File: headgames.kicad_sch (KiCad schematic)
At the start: 42 parts, among them J1 ELECTRODES, J2 9V ISOLATED BATTERY, U1 TLC274CN LOW-BIAS CMOS, U2 LM386

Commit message: Restore the inventory-first LM324N implementation
Undo the unavailable TLC274CN population decision while preserving the independently valid power-interface, alpha-band, detector, and verification improvements. Restore LM324N consistently across all five schematic units, the title block, README, and architectural guidance.

Make the inventory constraint executable by changing the root verification entrypoint to require LM324N for U1. Document its bipolar input-bias, offset, and noise limitations honestly at the 10 MΩ acquisition impedance, and retain a clean future replacement boundary without making an unstocked part mandatory for the MVP.

Verification: python3 manage.py test passes; KiCad ERC reports zero violations; native PDF export succeeds; git diff --check passes.
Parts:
- U1: value TLC274CN LOW-BIAS CMOS -> LM324N INVENTORY
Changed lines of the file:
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@@
 		(company "Headgames")
 		(comment 1 "BATTERY ONLY WHILE ELECTRODES ARE CONNECTED")
-		(comment 2 "TLC274CN reference, acquisition, alpha gain, and carrier")
+		(comment 2 "LM324N reference, acquisition, alpha gain, and carrier")
 		(comment 3 "Pins 1 and 8 of LM386 intentionally open for gain 20")
 		(comment 4 "Experimental prototype - not a medical device")
@@
 			)
 		)
-		(property "Value" "TLC274CN LOW-BIAS CMOS"
+		(property "Value" "LM324N INVENTORY"
 			(at 88.9 69.1896 0)
 			(effects
@@
 			)
 		)
-		(property "Value" "TLC274CN LOW-BIAS CMOS"
+		(property "Value" "LM324N INVENTORY"
 			(at 165.1 84.4296 0)
 			(effects
@@
 			)
 		)
-		(property "Value" "TLC274CN LOW-BIAS CMOS"
+		(property "Value" "LM324N INVENTORY"
 			(at 45.9232 82.423 0)
 			(effects
@@
 			)
 		)
-		(property "Value" "TLC274CN LOW-BIAS CMOS"
+		(property "Value" "LM324N INVENTORY"
 			(at 161.29 141.5796 0)
 			(effects
@@
 			)
 		)
-		(property "Value" "TLC274CN LOW-BIAS CMOS"
+		(property "Value" "LM324N INVENTORY"
 			(at 232.41 139.0396 0)
 			(effects

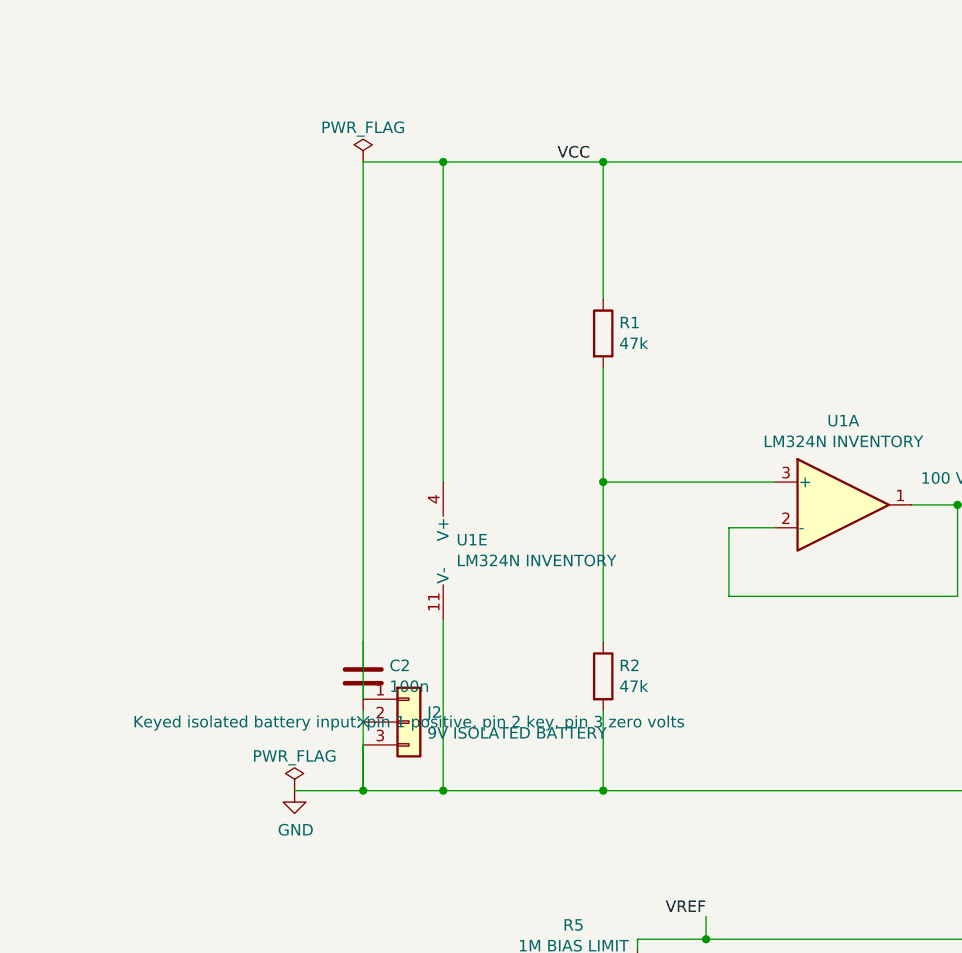
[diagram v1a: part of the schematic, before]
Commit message: Separate the battery inlet from supply decoupling
Move J2 into a dedicated inlet block at the far left of the schematic and route its positive and return conductors around the outside of the circuit. The keyed pin now has an isolated, visible no-connect marker, and neither battery conductor passes through a component body or field.

Restore C2 as an independent vertical bypass branch directly between VCC and ground. Shorten J2's displayed value to avoid colliding with C2 while retaining the complete polarity, keying, and isolation contract in the connector description and the on-sheet safety annotation.

Update the durable J2 value assertion to match the concise displayed field. Verification includes visual inspection of a fresh 3200-pixel native SVG render, successful PDF and netlist exports, zero KiCad ERC violations, passing root engineering checks, and git diff --check.
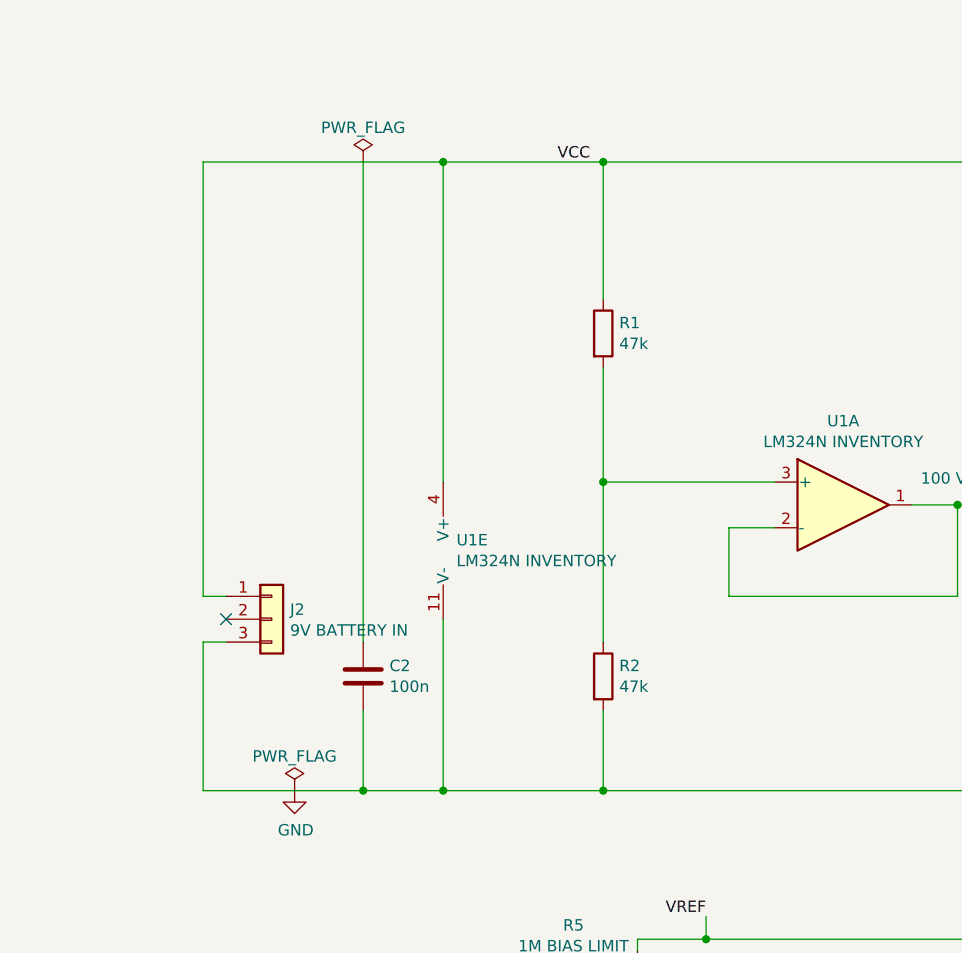
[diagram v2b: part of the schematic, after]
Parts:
- J2: value 9V ISOLATED BATTERY -> 9V BATTERY IN
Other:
- moved on the sheet: J2
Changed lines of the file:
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@@
 	)
 	(no_connect
-		(at 35.56 100.33)
+		(at 20.32 88.9)
 	)
 	(wire
 		(pts
-			(xy 35.56 91.44) (xy 35.56 97.79)
+			(xy 20.32 86.36) (xy 17.78 86.36)
 		)
 		(stroke (width 0) (type default))
@@
 	(wire
 		(pts
-			(xy 35.56 102.87) (xy 35.56 107.95)
+			(xy 17.78 86.36) (xy 17.78 38.1)
+		)
+		(stroke (width 0) (type default))
+	)
+	(wire
+		(pts
+			(xy 17.78 38.1) (xy 35.56 38.1)
+		)
+		(stroke (width 0) (type default))
+	)
+	(wire
+		(pts
+			(xy 20.32 91.44) (xy 17.78 91.44)
+		)
+		(stroke (width 0) (type default))
+	)
+	(wire
+		(pts
+			(xy 17.78 91.44) (xy 17.78 107.95)
+		)
+		(stroke (width 0) (type default))
+	)
+	(wire
+		(pts
+			(xy 17.78 107.95) (xy 27.94 107.95)
 		)
 		(stroke (width 0) (type default))
@@
 	(symbol
 		(lib_id "Connector_Generic:Conn_01x03")
-		(at 40.64 100.33 0)
+		(at 25.4 88.9 0)
 		(unit 1)
 		(exclude_from_sim no)
@@
 		(dnp no)
 		(property "Reference" "J2"
-			(at 42.672 99.2632 0)
+			(at 27.432 87.8332 0)
 			(effects (font (size 1.27 1.27)) (justify left))
 		)
-		(property "Value" "9V ISOLATED BATTERY"
-			(at 42.672 101.5746 0)
+		(property "Value" "9V BATTERY IN"
+			(at 27.432 90.1446 0)
 			(effects (font (size 1.27 1.27)) (justify left))
 		)
 		(property "Footprint" ""
-			(at 40.64 100.33 0)
+			(at 25.4 88.9 0)
 			(effects (font (size 1.27 1.27)))
 		)
 		(property "Datasheet" ""
-			(at 40.64 100.33 0)
+			(at 25.4 88.9 0)
 			(effects (font (size 1.27 1.27)))
 		)
 		(property "Description" "Keyed isolated battery input: pin 1 positive, pin 2 key, pin 3 zero volts"
-			(at 40.64 100.33 0)
-			(effects (font (size 1.27 1.27)))
+			(at 25.4 88.9 0)
+			(effects (font (size 1.27 1.27)) (hide yes))
 		)
 		(pin "1")

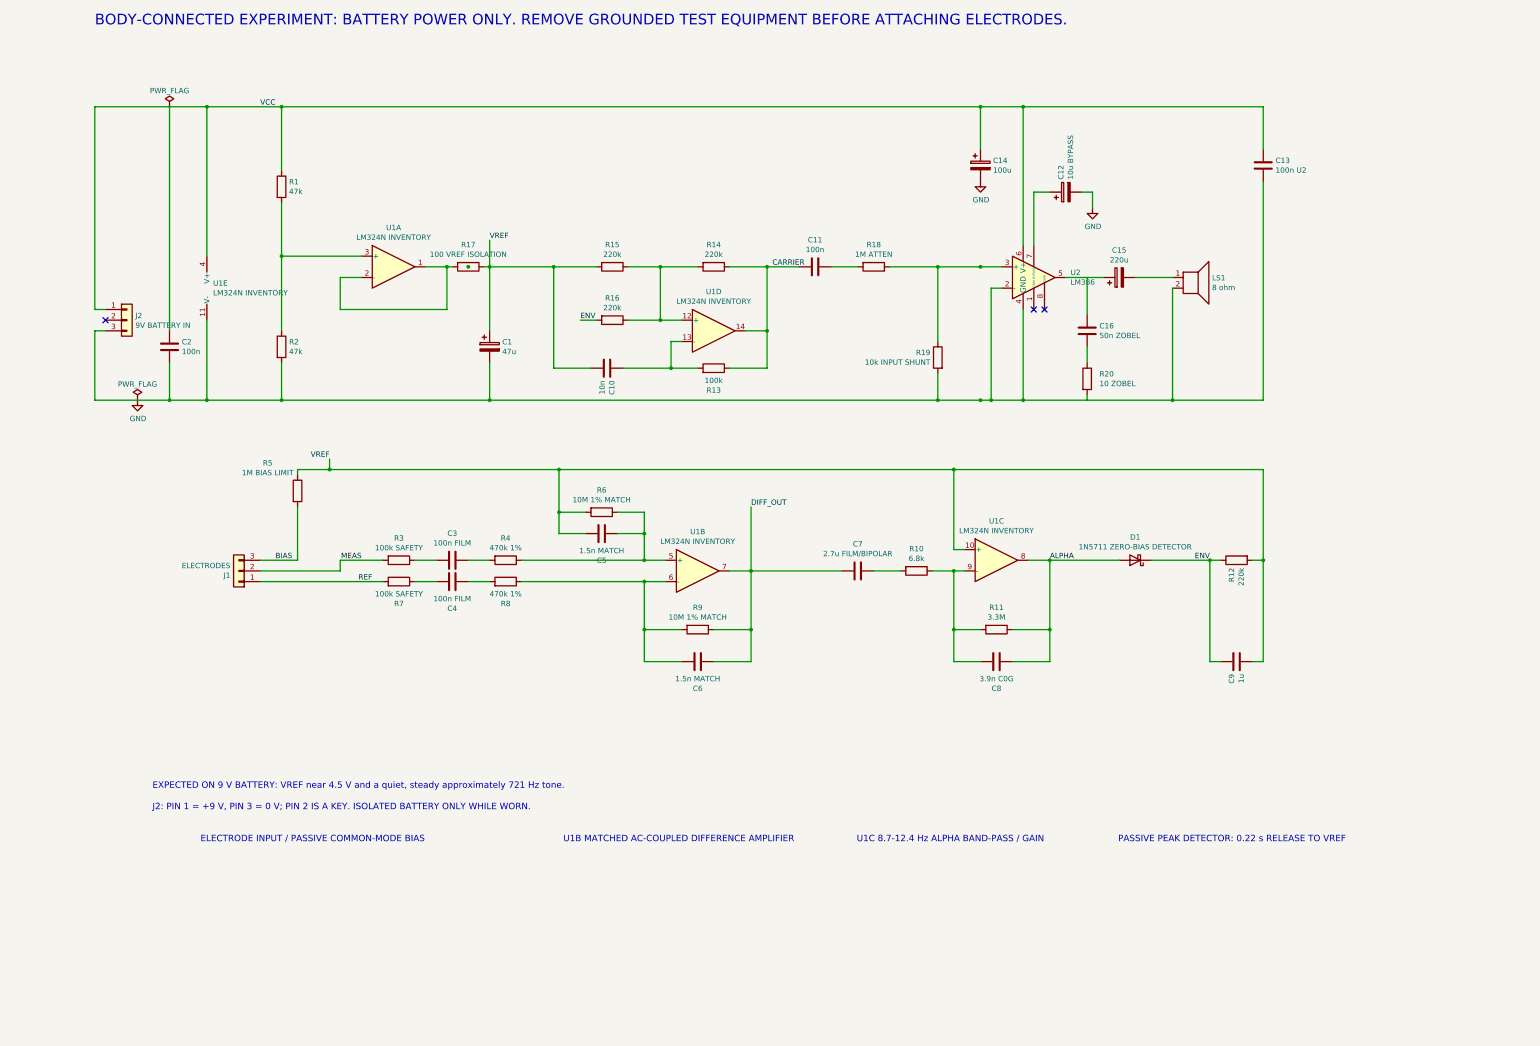
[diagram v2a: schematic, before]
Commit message: Replace the passive alpha detector with an LM358N precision stage
Use the inventory LM358N as a two-stage analog envelope front end. U3A now drives the existing 1N5711 inside its feedback loop so the op amp compensates the Schottky forward drop instead of requiring the filtered alpha signal to overcome it directly. Keep R12 and C9 as the authoritative 220 ms hold/release network referenced to VREF, and expose that held voltage as ENV_RAW.

Use U3B as a unity-gain buffer between ENV_RAW and the carrier-control input. This prevents the oscillator summing resistor from loading the detector capacitor while retaining an entirely analog feedback path. Add C17 as local 100 nF LM358N supply decoupling and preserve the isolated 9 V supply contract.

Extend manage.py with native-netlist assertions covering the complete precision-detector feedback topology, diode orientation, envelope buffer, power polarity, and local decoupling. Update README.md and AGENTS.md so the schematic, automated invariant checks, and architectural description agree.

Verified with python3 manage.py test, KiCad 9 ERC with zero violations, native KiCad XML netlist inspection, and git diff --check.
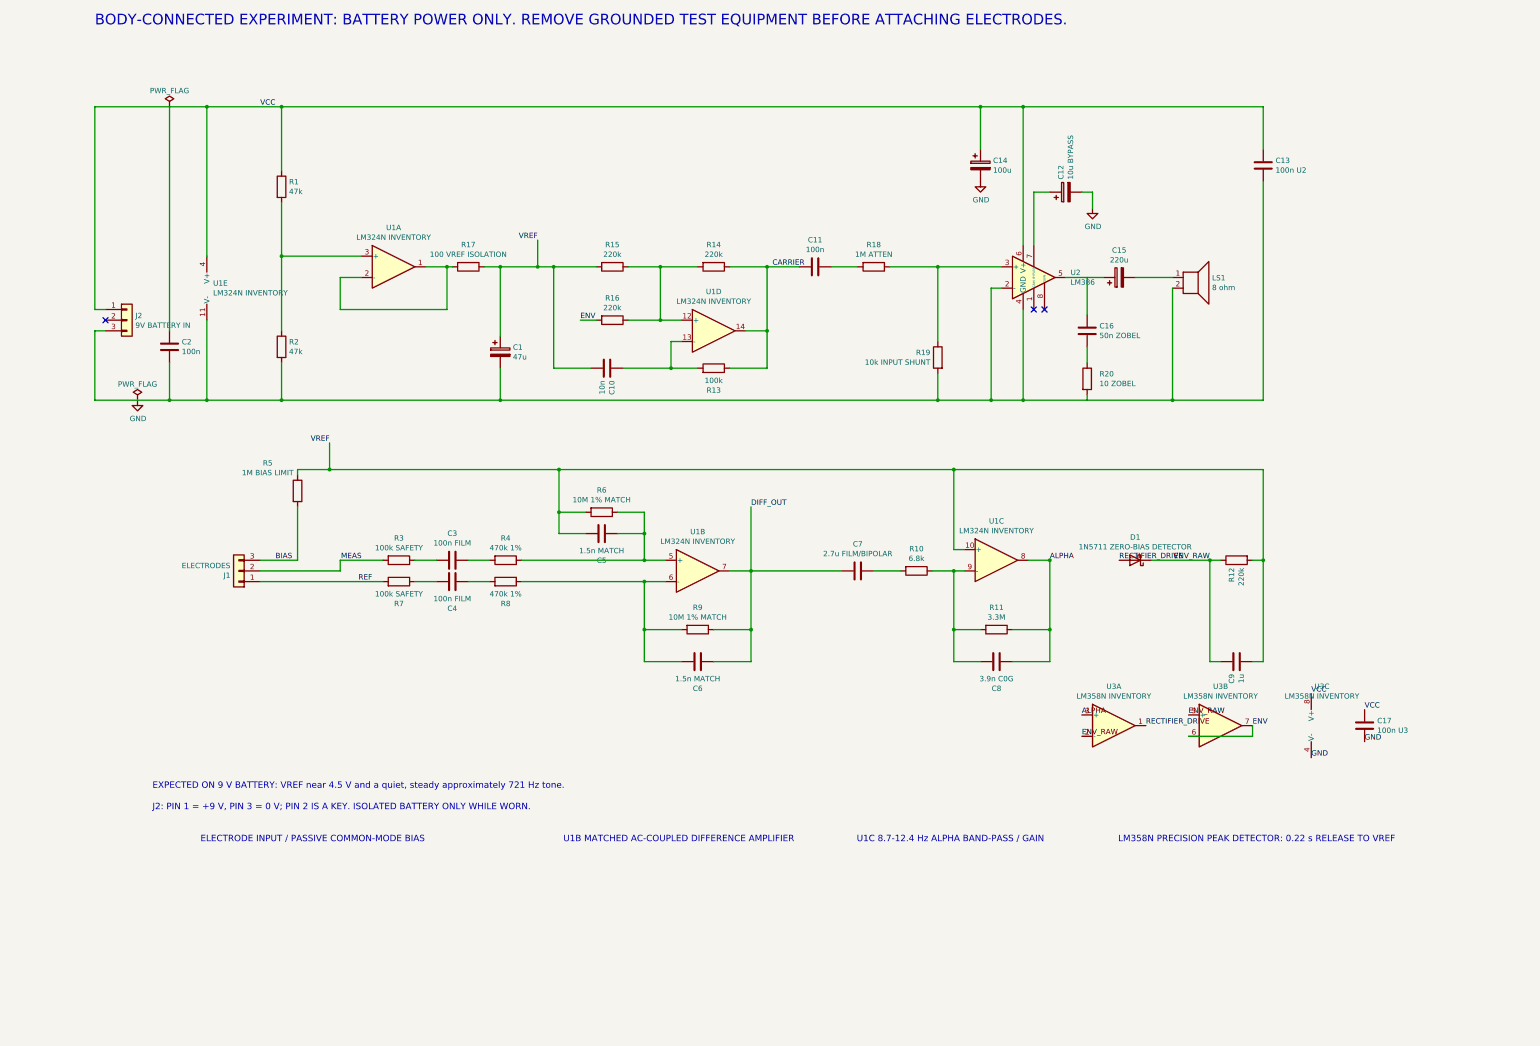
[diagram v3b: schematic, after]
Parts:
- added C17: 100n U3, symbol Device:C
- added U3: LM358N INVENTORY, symbol Amplifier_Operational:LM358
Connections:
- net ALPHA: now also U3.3 (+); no longer D1.2 (A)
- net ENV: now also U3.6 (-), U3.7; no longer C9.1, D1.1 (K), R12.1
- net GND: now also C17.2, U3.4 (V-)
- net VCC: now also C17.1, U3.8 (V+)
- new net ENV_RAW: C9.1, D1.1 (K), R12.1, U3.2 (-), U3.5 (+)
- new net RECTIFIER_DRIVE: D1.2 (A), U3.1
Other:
- note added: "LM358N PRECISION PEAK DETECTOR: 0.22 s RELEASE TO VREF"
- note removed: "PASSIVE PEAK DETECTOR: 0.22 s RELEASE TO VREF"
- moved on the sheet: C1
